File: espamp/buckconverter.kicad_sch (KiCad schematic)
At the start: 1 part, among them U401 TPS54202DDC

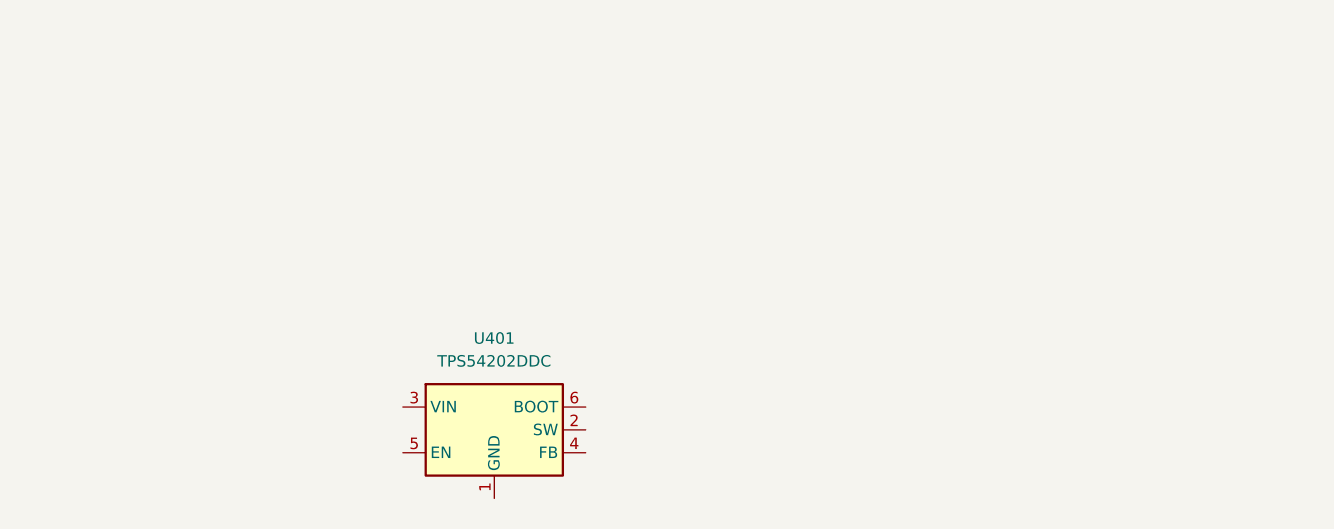
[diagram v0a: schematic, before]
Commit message: initial buckconverter with pcb
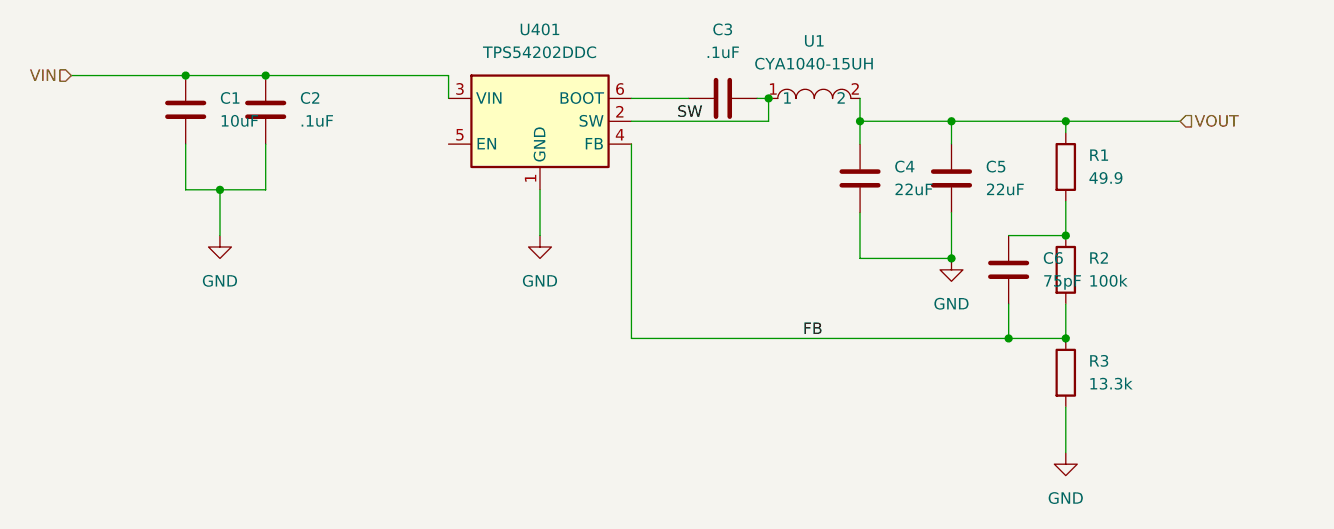
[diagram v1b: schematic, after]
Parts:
- added C1: 10uF, Capacitor_SMD:C_0603_1608Metric, symbol Device:C
- added C2, C3: .1uF, Capacitor_SMD:C_0603_1608Metric, symbol Device:C
- added C4, C5: 22uF, Capacitor_SMD:C_0603_1608Metric, symbol Device:C
- added C6: 75pF, Capacitor_SMD:C_0603_1608Metric, symbol Device:C
- added R1: 49.9, Resistor_SMD:R_0603_1608Metric, symbol Device:R
- added R2: 100k, Resistor_SMD:R_0603_1608Metric, symbol Device:R
- added R3: 13.3k, Resistor_SMD:R_0603_1608Metric, symbol Device:R
- added U1: CYA1040-15UH, easyeda2kicad:IND-SMD_L11.6-W10.1, symbol easyeda2kicad:CYA1040-15UH
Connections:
- net GND: now reaches U401.1 (GND)
- net GND: now also C1.2, C2.2, C4.1, C5.2, R3.2
- net SW: now reaches U401.2 (SW)
- net SW: now also C3.2, U1.1
- net VIN: now reaches U401.3 (VIN)
- net VIN: now also C1.1, C2.1
- net FB: now reaches U401.4 (FB)
- net FB: now also C6.1, R2.2, R3.1
- net at U401.6 (BOOT): now also C3.1
- new net: C6.2, R1.2, R2.1
- new net VOUT: C4.2, C5.1, R1.1, U1.2
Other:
- moved on the sheet: U401

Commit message: Clean up the BOM  - use whole numbers (.1uF -> 100nF)  - capacitor voltage ratings ([22uF](https://jlcpcb.com/partdetail/PANASONIC-EEEFT1H220AR/C336246) at 50V)
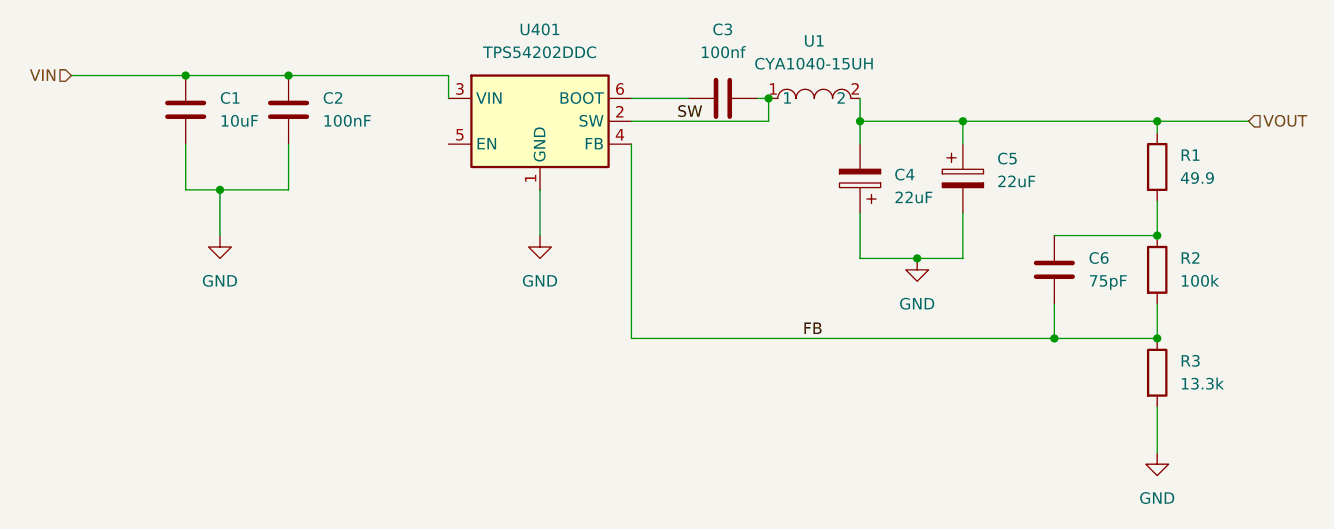
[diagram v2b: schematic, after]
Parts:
- C2: value .1uF -> 100nF
- C3: value .1uF -> 100nf
- C4, C5: footprint Capacitor_SMD:C_0603_1608Metric -> Capacitor_SMD:C_Elec_5x5.8; symbol Device:C -> Device:C_Polarized
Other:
- moved on the sheet: C2, C6, R1, R2, R3

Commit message: clean up layout
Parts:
- C4, C5: LCSC Part (none) -> C336246
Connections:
- net GND: now also C4.2; no longer C4.1
- net VOUT: now also C4.1; no longer C4.2
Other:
- moved on the sheet: C4
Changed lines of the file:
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@@
+			)
+		)
+		(property "Label" ""
+			(at 120.65 36.83 0)
+			(effects
+				(font
+					(size 1.27 1.27)
+				)
+				(hide yes)
+			)
+		)
+		(property "LCSC Part" "C336246"
+			(at 120.65 36.83 0)
+			(effects
+				(font
+					(size 1.27 1.27)
+				)
+				(hide yes)
 			)
 		)
@@
 	(symbol
 		(lib_id "Device:C_Polarized")
-		(at 109.22 36.83 180)
+		(at 109.22 36.83 0)
 		(unit 1)
 		(exclude_from_sim no)
@@
 		(fields_autoplaced yes)
 		(property "Reference" "C4"
-			(at 113.03 36.4489 0)
-			(effects
-				(font
-					(size 1.27 1.27)
-				)
-				(justify right)
+			(at 113.03 34.6709 0)
+			(effects
+				(font
+					(size 1.27 1.27)
+				)
+				(justify left)
 			)
 		)
 		(property "Value" "22uF"
-			(at 113.03 38.9889 0)
-			(effects
-				(font
-					(size 1.27 1.27)
-				)
-				(justify right)
+			(at 113.03 37.2109 0)
+			(effects
+				(font
+					(size 1.27 1.27)
+				)
+				(justify left)
 			)
 		)
 		(property "Footprint" "Capacitor_SMD:C_Elec_5x5.8"
-			(at 108.2548 33.02 0)
+			(at 110.1852 40.64 0)
 			(effects
 				(font
@@
 			(at 109.22 36.83 0)
 			(effects
+				(font
+					(size 1.27 1.27)
+				)
+				(hide yes)
+			)
+		)
+		(property "Label" ""
+			(at 109.22 36.83 0)
+			(effects
+				(font
+					(size 1.27 1.27)
+				)
+				(hide yes)
+			)
+		)
+		(property "LCSC Part" "C336246"
+			(at 109.22 36.83 0)
+			(effects

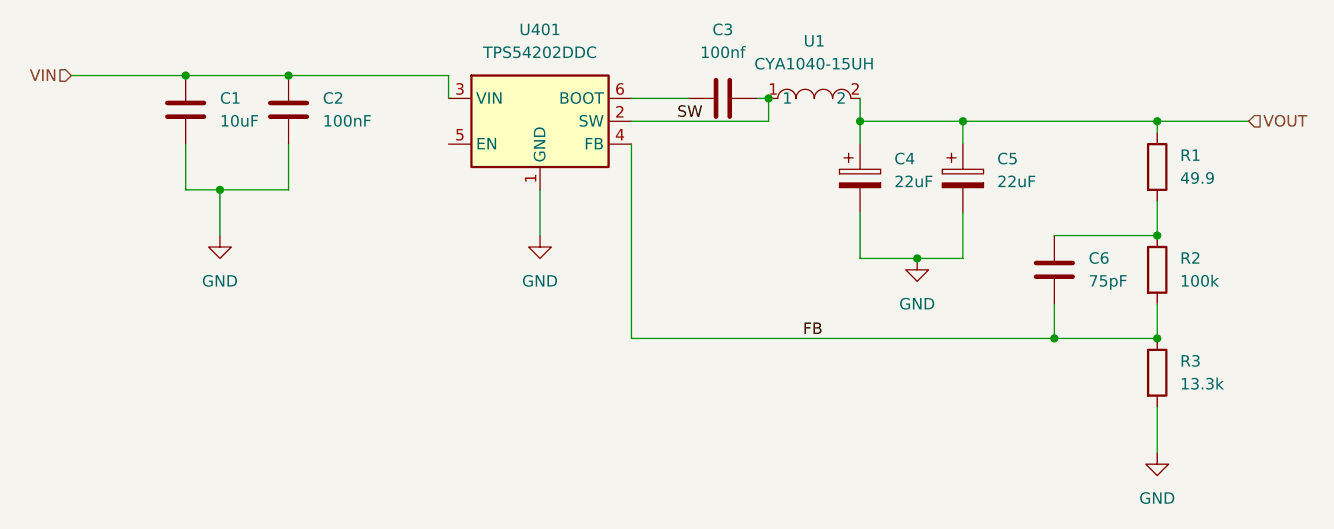
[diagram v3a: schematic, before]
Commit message: amp schematic complete
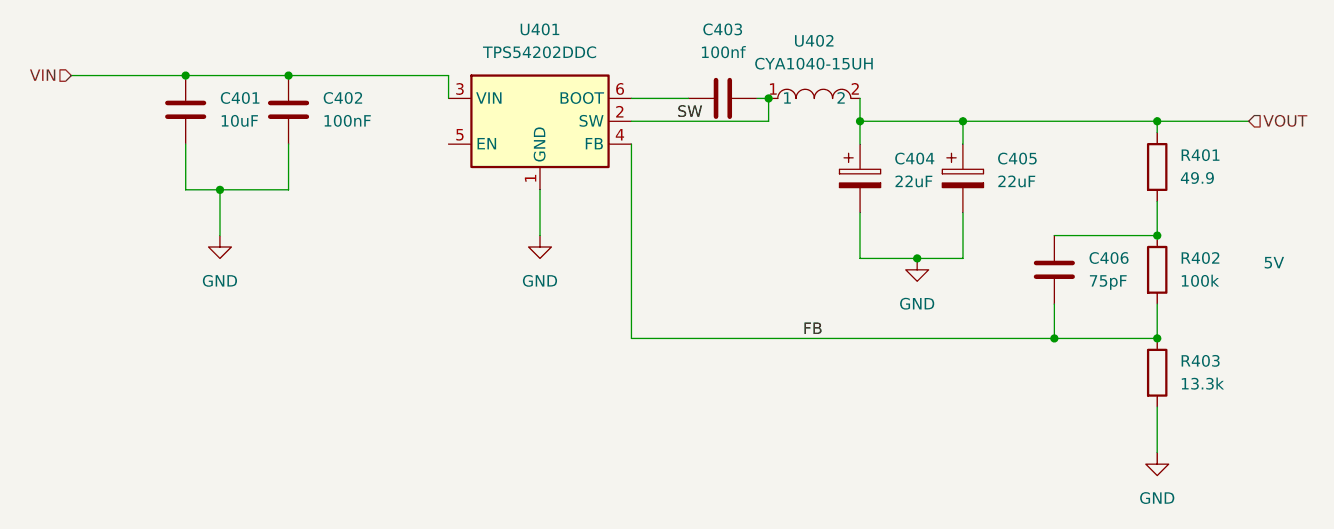
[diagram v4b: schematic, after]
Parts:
- renumbered C1 to C401, C2 to C402, C3 to C403, C4 to C404, C5 to C405, C6 to C406, R1 to R401, R2 to R402, R3 to R403, U1 to U402
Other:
- note added: "5V"
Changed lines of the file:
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@@
 		)
 	)
-	(label "FB"
-		(at 102.87 54.61 0)
-		(fields_autoplaced yes)
+	(text "5V"
+		(exclude_from_sim no)
+		(at 155.194 46.482 0)
 		(effects
 			(font
 				(size 1.27 1.27)
 			)
-			(justify left bottom)
-		)
-	)
-	(label "SW"
-		(at 88.9 30.48 0)
-		(fields_autoplaced yes)
+		)
+	)
+	(label "FB"
+		(at 102.87 54.61 0)
 		(effects
 			(font
@@
 		)
 	)
+	(label "SW"
+		(at 88.9 30.48 0)
+		(effects
+			(font
+				(size 1.27 1.27)
+			)
+			(justify left bottom)
+		)
+	)
 	(hierarchical_label "VIN"
 		(shape input)
 		(at 21.59 25.4 180)
-		(fields_autoplaced yes)
 		(effects
 			(font
@@
 		(shape input)
 		(at 152.4 30.48 0)
-		(fields_autoplaced yes)
 		(effects
 			(font
@@
 		(dnp no)
 		(fields_autoplaced yes)
-		(property "Reference" "#PWR04"
+		(property "Reference" "#PWR0404"
 			(at 142.24 73.66 0)
 			(effects
@@
 			(project ""
 				(path "/48ddfdd8-68fa-4e63-aa18-bc113cdf8cfa/aa9739d0-05d8-4c74-a4fd-846c263eed0b"
-					(reference "#PWR04")
+					(reference "#PWR0404")
 					(unit 1)
 				)
@@
 		(dnp no)
 		(fields_autoplaced yes)
-		(property "Reference" "#PWR02"
+		(property "Reference" "#PWR0401"
 			(at 38.1 49.53 0)
 			(effects
@@
 			(project ""
 				(path "/48ddfdd8-68fa-4e63-aa18-bc113cdf8cfa/aa9739d0-05d8-4c74-a4fd-846c263eed0b"
-					(reference "#PWR02")
+					(reference "#PWR0401")
 					(unit 1)
 				)
@@
 		(dnp no)
 		(fields_autoplaced yes)
-		(property "Reference" "R2"
+		(property "Reference" "R402"
 			(at 144.78 45.7199 0)
 			(effects
@@
 			(project ""
 				(path "/48ddfdd8-68fa-4e63-aa18-bc113cdf8cfa/aa9739d0-05d8-4c74-a4fd-846c263eed0b"
-					(reference "R2")
+					(reference "R402")
 					(unit 1)
 				)
@@
 		(dnp no)
 		(fields_autoplaced yes)
-		(property "Reference" "C6"
+		(property "Reference" "C406"
 			(at 134.62 45.7199 0)
 			(effects
@@
 			(project ""
 				(path "/48ddfdd8-68fa-4e63-aa18-bc113cdf8cfa/aa9739d0-05d8-4c74-a4fd-846c263eed0b"
-					(reference "C6")
+					(reference "C406")
 					(unit 1)
 				)
@@
 		(dnp no)
 		(fields_autoplaced yes)
-		(property "Reference" "C2"
+		(property "Reference" "C402"
 			(at 49.53 27.9399 0)
 			(effects
@@
 			(project ""
 				(path "/48ddfdd8-68fa-4e63-aa18-bc113cdf8cfa/aa9739d0-05d8-4c74-a4fd-846c263eed0b"
-					(reference "C2")
+					(reference "C402")
 					(unit 1)
 				)
@@
 		(dnp no)
 		(fields_autoplaced yes)
-		(property "Reference" "R1"
+		(property "Reference" "R401"
 			(at 144.78 34.2899 0)
 			(effects
@@
 			(project ""
 				(path "/48ddfdd8-68fa-4e63-aa18-bc113cdf8cfa/aa9739d0-05d8-4c74-a4fd-846c263eed0b"
-					(reference "R1")
+					(reference "R401")
 					(unit 1)
 				)
@@
 		(dnp no)
 		(fields_autoplaced yes)
-		(property "Reference" "C1"
+		(property "Reference" "C401"
 			(at 38.1 27.9399 0)
 			(effects
@@
 			(project ""
 				(path "/48ddfdd8-68fa-4e63-aa18-bc113cdf8cfa/aa9739d0-05d8-4c74-a4fd-846c263eed0b"
-					(reference "C1")
+					(reference "C401")
 					(unit 1)
 				)
@@
 		(dnp no)
 		(fields_autoplaced yes)
-		(property "Reference" "#PWR03"
+		(property "Reference" "#PWR0403"
 			(at 115.57 52.07 0)
 			(effects
@@
 			(project ""
 				(path "/48ddfdd8-68fa-4e63-aa18-bc113cdf8cfa/aa9739d0-05d8-4c74-a4fd-846c263eed0b"
-					(reference "#PWR03")
+					(reference "#PWR0403")
 					(unit 1)
 				)
@@
 		(dnp no)
 		(fields_autoplaced yes)
-		(property "Reference" "C5"
+		(property "Reference" "C405"
 			(at 124.46 34.6709 0)
 			(effects
@@
 			(project ""
 				(path "/48ddfdd8-68fa-4e63-aa18-bc113cdf8cfa/aa9739d0-05d8-4c74-a4fd-846c263eed0b"
-					(reference "C5")
+					(reference "C405")
 					(unit 1)
 				)
@@
 		(dnp no)
 		(fields_autoplaced yes)
-		(property "Reference" "U1"
+		(property "Reference" "U402"
 			(at 104.14 21.59 0)
 			(effects
@@
 			(project ""
 				(path "/48ddfdd8-68fa-4e63-aa18-bc113cdf8cfa/aa9739d0-05d8-4c74-a4fd-846c263eed0b"
-					(reference "U1")
+					(reference "U402")
 					(unit 1)
 				)
@@
 		(dnp no)
 		(fields_autoplaced yes)
-		(property "Reference" "C3"
+		(property "Reference" "C403"
 			(at 93.98 20.32 90)
 			(effects
@@
 			(project ""
 				(path "/48ddfdd8-68fa-4e63-aa18-bc113cdf8cfa/aa9739d0-05d8-4c74-a4fd-846c263eed0b"
-					(reference "C3")
+					(reference "C403")
 					(unit 1)
 				)
@@
 		(dnp no)
 		(fields_autoplaced yes)
-		(property "Reference" "C4"
+		(property "Reference" "C404"
 			(at 113.03 34.6709 0)
 			(effects
@@
 			(project ""
 				(path "/48ddfdd8-68fa-4e63-aa18-bc113cdf8cfa/aa9739d0-05d8-4c74-a4fd-846c263eed0b"
-					(reference "C4")
+					(reference "C404")
 					(unit 1)
 				)
@@
 		(dnp no)
 		(fields_autoplaced yes)
-		(property "Reference" "R3"
+		(property "Reference" "R403"
 			(at 144.78 57.1499 0)
 			(effects
@@
 			(project ""
 				(path "/48ddfdd8-68fa-4e63-aa18-bc113cdf8cfa/aa9739d0-05d8-4c74-a4fd-846c263eed0b"
-					(reference "R3")
+					(reference "R403")
 					(unit 1)
 				)
@@
 		(dnp no)
 		(fields_autoplaced yes)
-		(property "Reference" "#PWR01"
+		(property "Reference" "#PWR0402"
 			(at 73.66 49.53 0)
 			(effects
@@
 			(project ""
 				(path "/48ddfdd8-68fa-4e63-aa18-bc113cdf8cfa/aa9739d0-05d8-4c74-a4fd-846c263eed0b"
-					(reference "#PWR01")
-					(unit 1)
-				)
+					(reference "#PWR0402")
+					(unit 1)
+				)

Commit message: espamp revisions
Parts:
- added TP401: LabeledTestPoint, easyeda2kicad:LabeledTestPoint, symbol easyeda2kicad:LabeledTestPoint
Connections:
- net VOUT: now also TP401.1
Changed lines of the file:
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@@
+	)
+	(junction
+		(at 134.62 30.48)
+		(diameter 0)
+		(color 0 0 0 0)
 	)
 	(junction
@@
 	(wire
 		(pts
-			(xy 120.65 30.48) (xy 142.24 30.48)
+			(xy 120.65 30.48) (xy 134.62 30.48)
 		)
 		(stroke
@@
 		(pts
 			(xy 21.59 25.4) (xy 34.29 25.4)
+		)
+		(stroke
+			(width 0)
+			(type default)
+		)
+	)
+	(wire
+		(pts
+			(xy 134.62 30.48) (xy 142.24 30.48)
 		)
 		(stroke
@@
 	(label "FB"
 		(at 102.87 54.61 0)
+		(fields_autoplaced yes)
 		(effects
 			(font
@@
 	(label "SW"
 		(at 88.9 30.48 0)
+		(fields_autoplaced yes)
 		(effects
 			(font
@@
 		(shape input)
 		(at 21.59 25.4 180)
+		(fields_autoplaced yes)
 		(effects
 			(font
@@
 		(shape input)
 		(at 152.4 30.48 0)
+		(fields_autoplaced yes)
 		(effects
 			(font
@@
 					(unit 1)
 				)
+			)
+		)
+	)
+	(symbol
+		(lib_id "easyeda2kicad:LabeledTestPoint")
+		(at 134.62 30.48 0)
+		(unit 1)
+		(exclude_from_sim no)
+		(in_bom no)
+		(on_board yes)
+		(dnp no)
+		(fields_autoplaced yes)
+		(property "Reference" "TP401"
+			(at 134.62 23.622 0)
+			(effects
+				(font
+					(size 1.27 1.27)
+				)
+				(hide yes)
+			)
+		)
+		(property "Value" "LabeledTestPoint"
+			(at 134.62 25.4 0)
+			(effects
+				(font
+					(size 1.27 1.27)
+				)
+				(hide yes)
+			)
+		)
+		(property "Footprint" "easyeda2kicad:LabeledTestPoint"
+			(at 139.7 30.48 0)
+			(effects
+				(font
+					(size 1.27 1.27)
+				)
+				(hide yes)
+			)
+		)
+		(property "Datasheet" "~"
+			(at 139.7 30.48 0)
+			(effects
+				(font
+					(size 1.27 1.27)
+				)
+				(hide yes)
+			)
+		)
+		(property "Description" "test point"
+			(at 134.62 30.48 0)
+			(effects
+				(font
+					(size 1.27 1.27)
+				)
+				(hide yes)
+			)
+		)
+		(property "Label" "5V"
+			(at 137.16 27.1779 0)
+			(effects
+				(font
+					(size 1.27 1.27)
+				)
+				(justify left)
+			)
+		)
+		(pin "1"
+		)
+		(instances
+			(project "espamp"
+				(path "/48ddfdd8-68fa-4e63-aa18-bc113cdf8cfa/aa9739d0-05d8-4c74-a4fd-846c263eed0b"
+					(reference "TP401")
+					(unit 1)
+				)
